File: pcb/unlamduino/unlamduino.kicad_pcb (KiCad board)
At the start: 2 copper layers, 106.7 x 69.8 mm, 41 parts, among them IC2 ATMEGA328-P, P3 CONN_01X08, U1 LM2576, U2 AP111733, Y2 16MHz

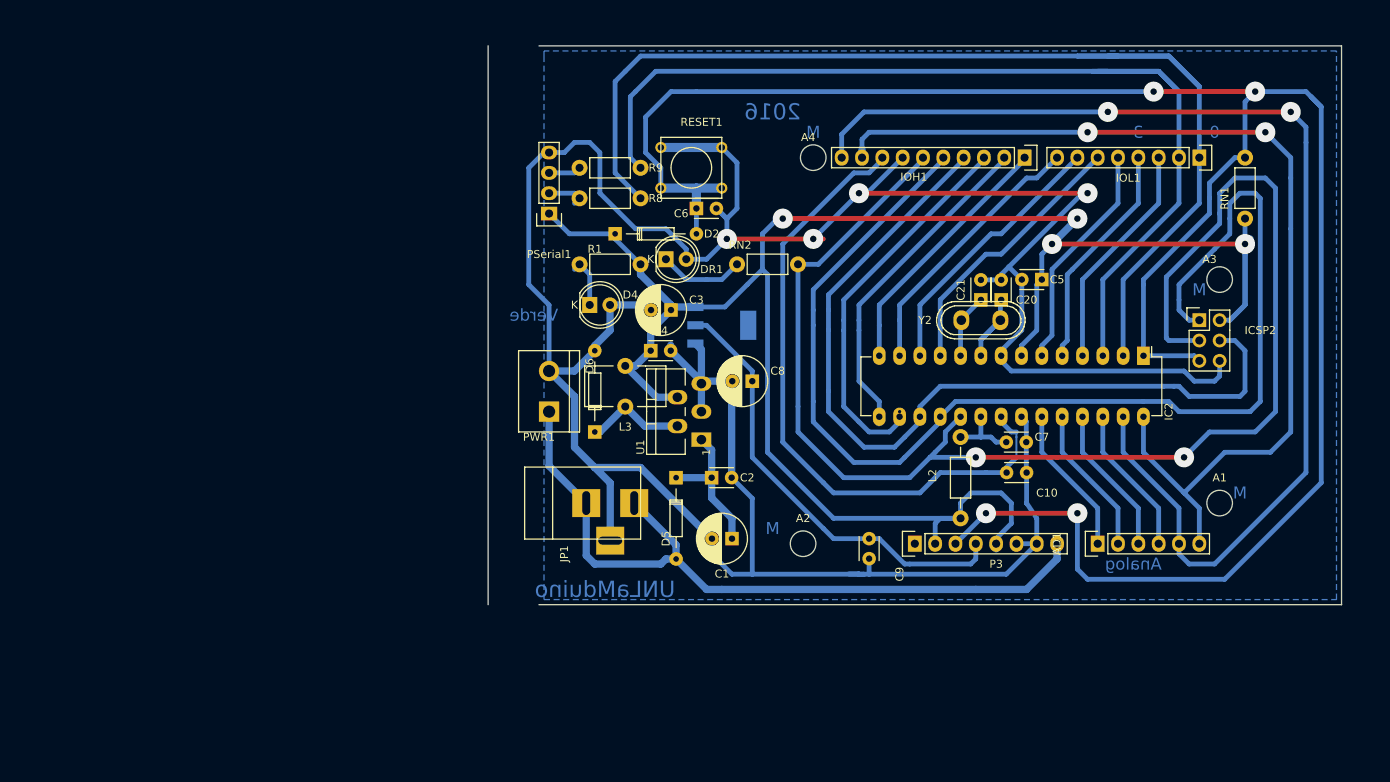
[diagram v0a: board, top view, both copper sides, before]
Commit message: Agregado agujeros de fijación y borde de relleno.
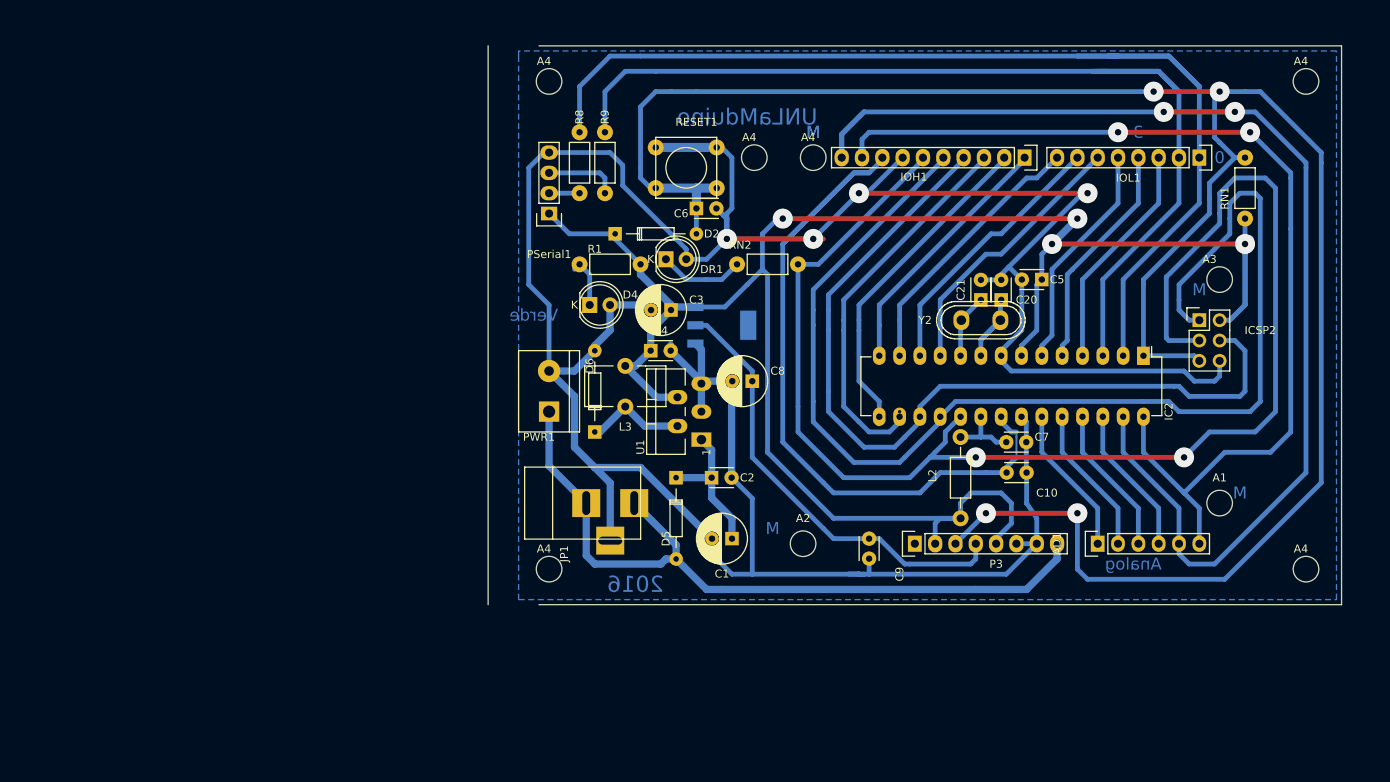
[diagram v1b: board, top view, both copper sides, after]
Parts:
- added A4: Agujero, Mounting_Holes:MountingHole_3.2mm_M3, F.Cu at (254.0, 104.1)
- added A4: Agujero, Mounting_Holes:MountingHole_3.2mm_M3, F.Cu at (159.4, 104.1)
- added A4: Agujero, Mounting_Holes:MountingHole_3.2mm_M3, F.Cu at (185.0, 52.7)
- added A4: Agujero, Mounting_Holes:MountingHole_3.2mm_M3, F.Cu at (159.4, 43.2)
- added A4: Agujero, Mounting_Holes:MountingHole_3.2mm_M3, F.Cu at (254.0, 43.2)
- moved R8 11.2 mm to (163.2, 49.5), turned to 270 degrees
- moved R9 6.29 mm to (166.4, 49.5), turned to 270 degrees
- moved RESET1 0.63 mm to (176.5, 54.0)
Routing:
- net /AD4/SDA: track 147.3 -> 165.3 mm
- net /AREF: track 82.1 -> 96.6 mm
- net /IO0: track 148.2 -> 142.7 mm
- net Net-(PSerial1-Pad3): track 4.07 -> 9.15 mm
- net /RESET: track 265.6 -> 263.0 mm
- net /IO1: track 130.4 -> 129.0 mm
- net Net-(PSerial1-Pad2): track 4.97 -> 3.81 mm
- net /AD5/SCL: track 128.1 -> 127.0 mm

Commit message: Correccion de algunas pistas cerca de islas y limpieza de pistas solapadas.
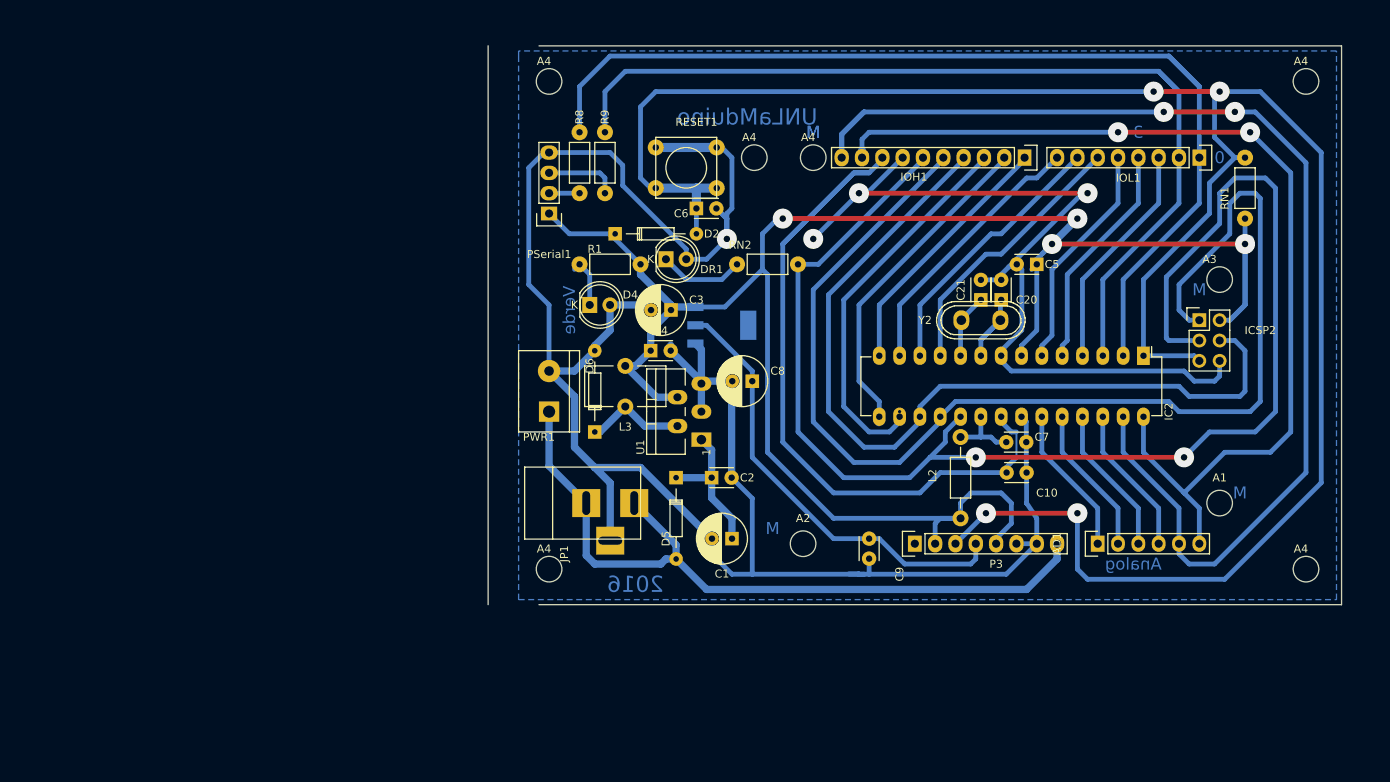
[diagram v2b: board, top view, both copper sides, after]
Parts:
- moved C5 2.01 mm to (220.3, 66.0)
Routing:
- net /IO0: track 142.7 -> 130.0 mm
- net GND: track 391.2 -> 380.1 mm
- net /IO1: track 129.0 -> 119.5 mm
- net /VIN: track 108.6 -> 101.0 mm
- net +5V: track 245.4 -> 248.1 mm

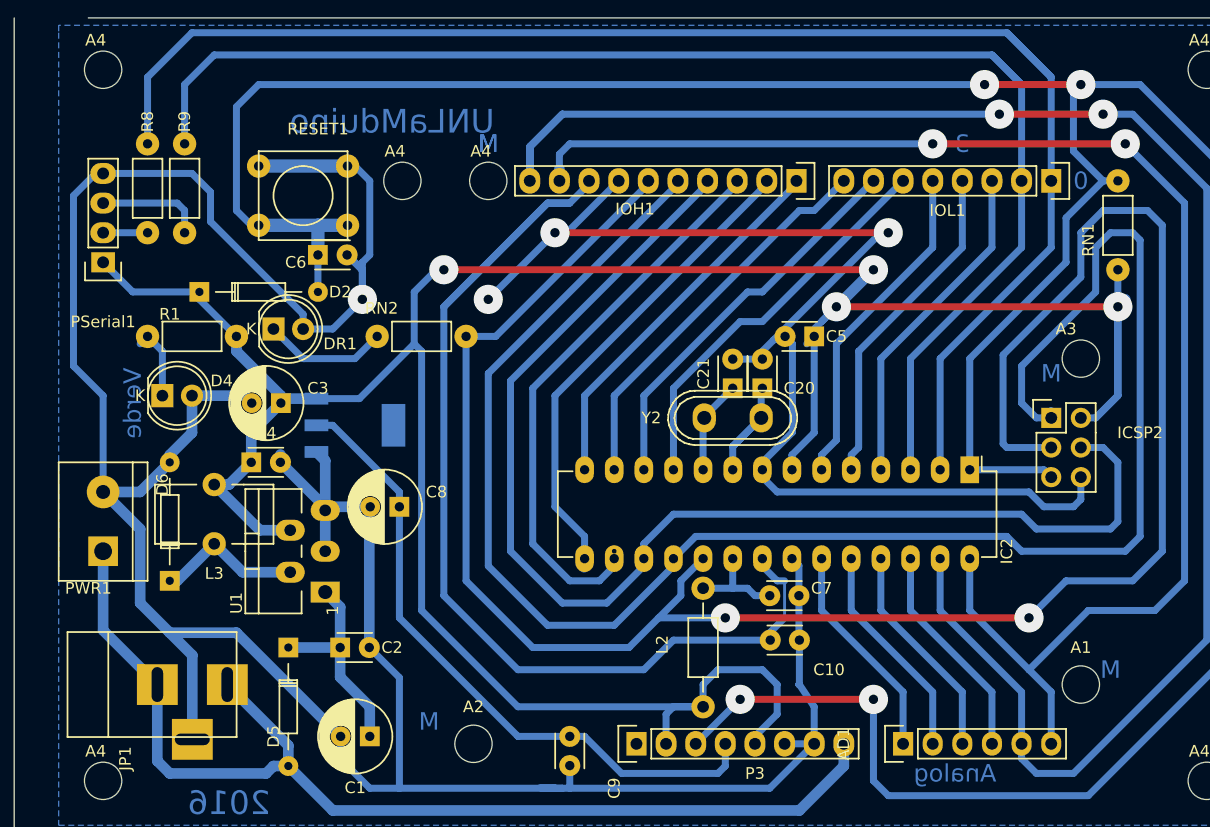
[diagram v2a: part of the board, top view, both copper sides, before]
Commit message: Capacitor mas ancho por pista por el medio y acomodado de alguna pista.
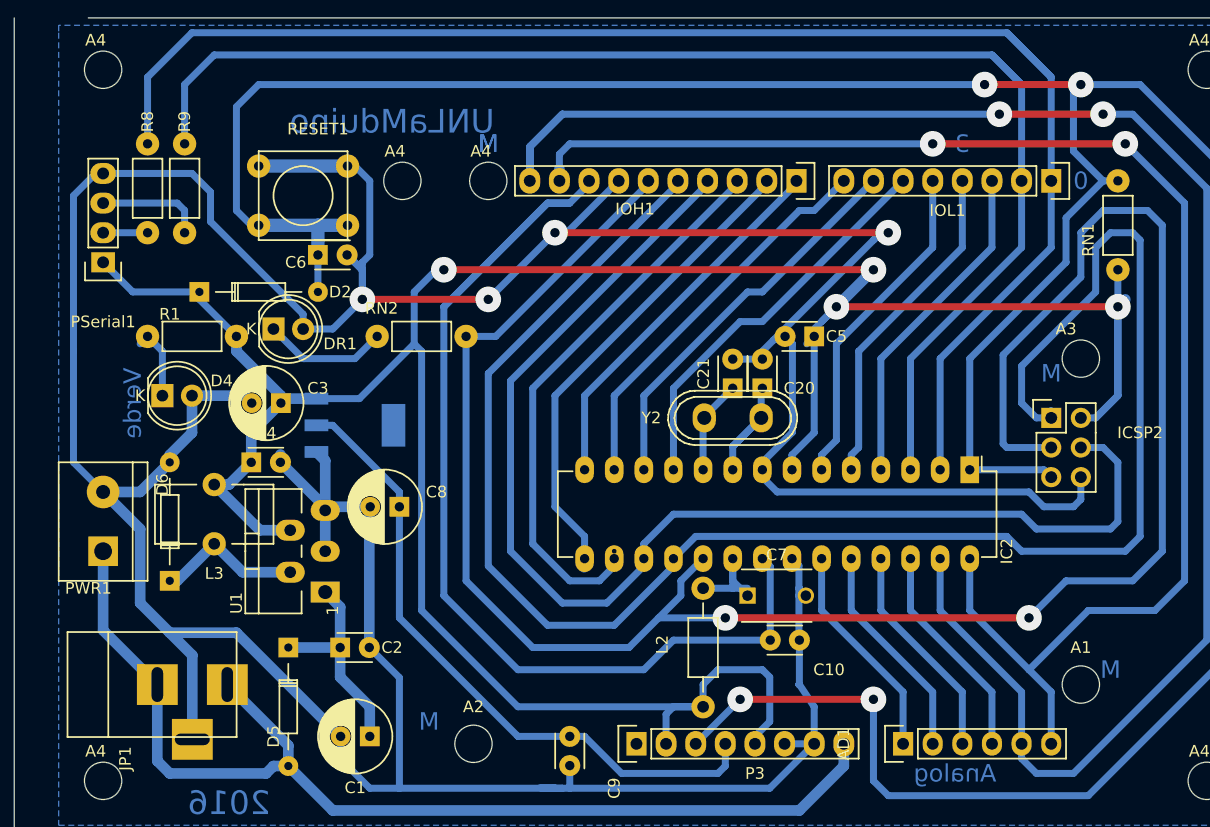
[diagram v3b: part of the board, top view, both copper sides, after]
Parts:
- C7: footprint Capacitors_ThroughHole:C_Disc_D3_P2.5 -> Capacitors_ThroughHole:C_Disc_D6_P5
- moved C7 1.91 mm to (214.6, 88.3)
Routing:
- net GND: track 380.1 -> 393.1 mm
- net Net-(C7-Pad1): track 9.15 -> 10.7 mm
- net +5V: track 248.1 -> 247.0 mm
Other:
- net class Default: via_dia 2.5 -> 2.2

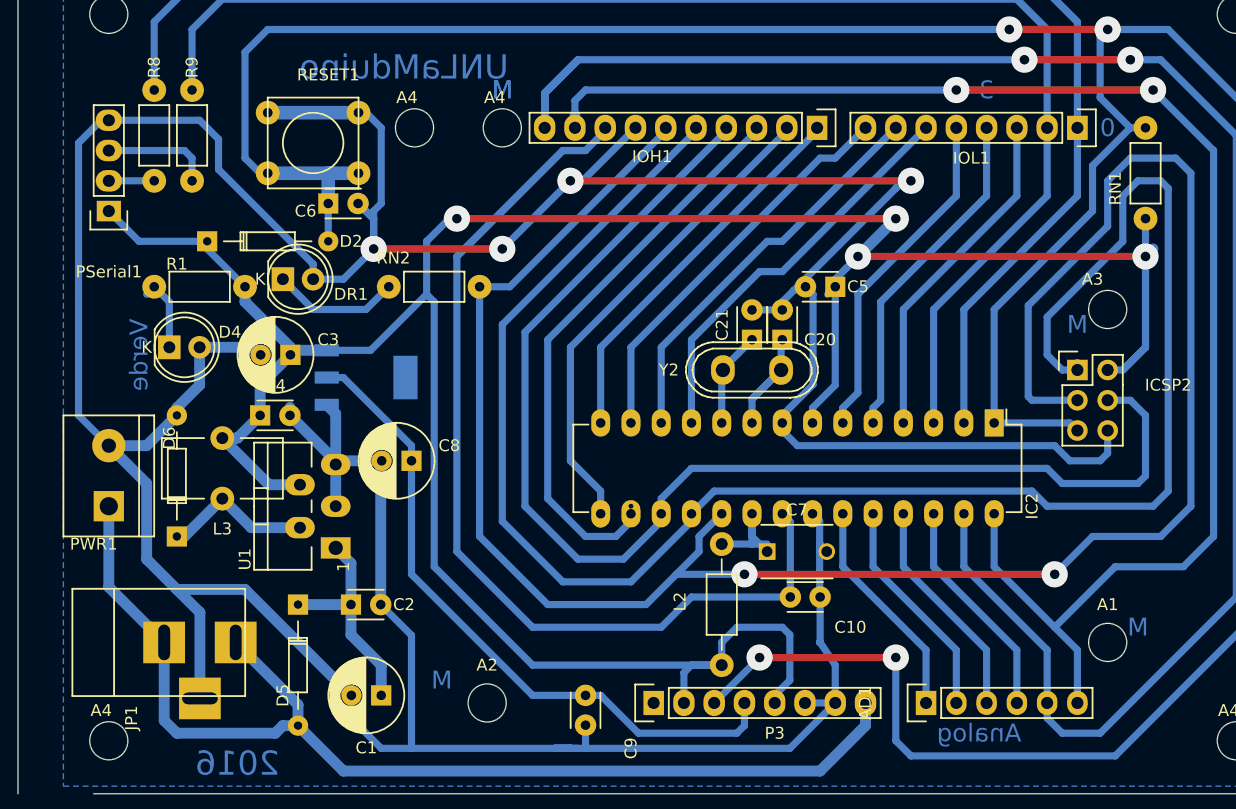
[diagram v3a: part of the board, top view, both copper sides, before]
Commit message: Conector de alimentacion corrido para lugar de agujero.
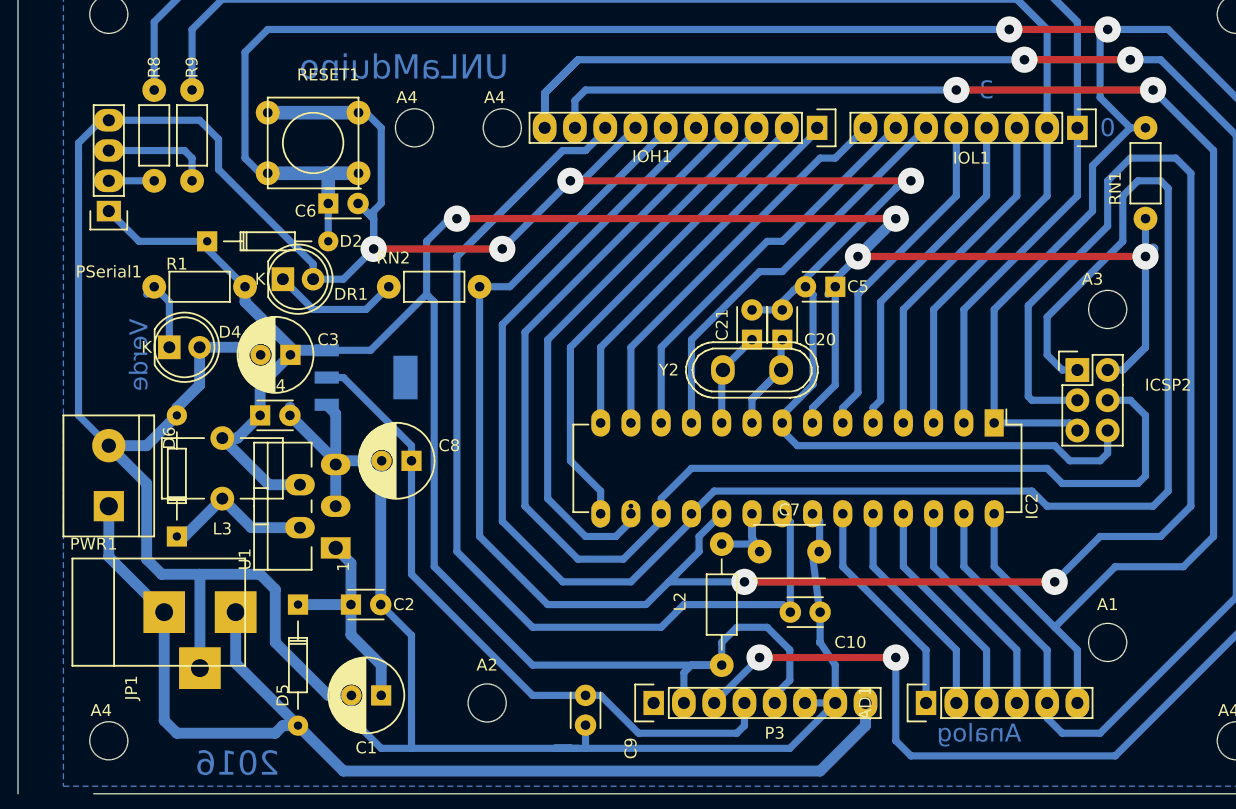
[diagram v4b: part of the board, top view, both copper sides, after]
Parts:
- moved JP1 2.54 mm to (163.8, 93.3)
- moved C10 1.27 mm to (219.1, 93.3)
- moved C7 0.63 mm to (214.0, 88.3)
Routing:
- net /VIN: track 101.0 -> 103.5 mm
- net /AREF: track 96.5 -> 97.8 mm
- net GND: track 393.1 -> 394.3 mm
- net Net-(C7-Pad1): track 10.7 -> 9.67 mm
- net /IO13: track 176.4 -> 177.3 mm
- net +5V: track 247.0 -> 246.2 mm
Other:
- board text removed: "M"

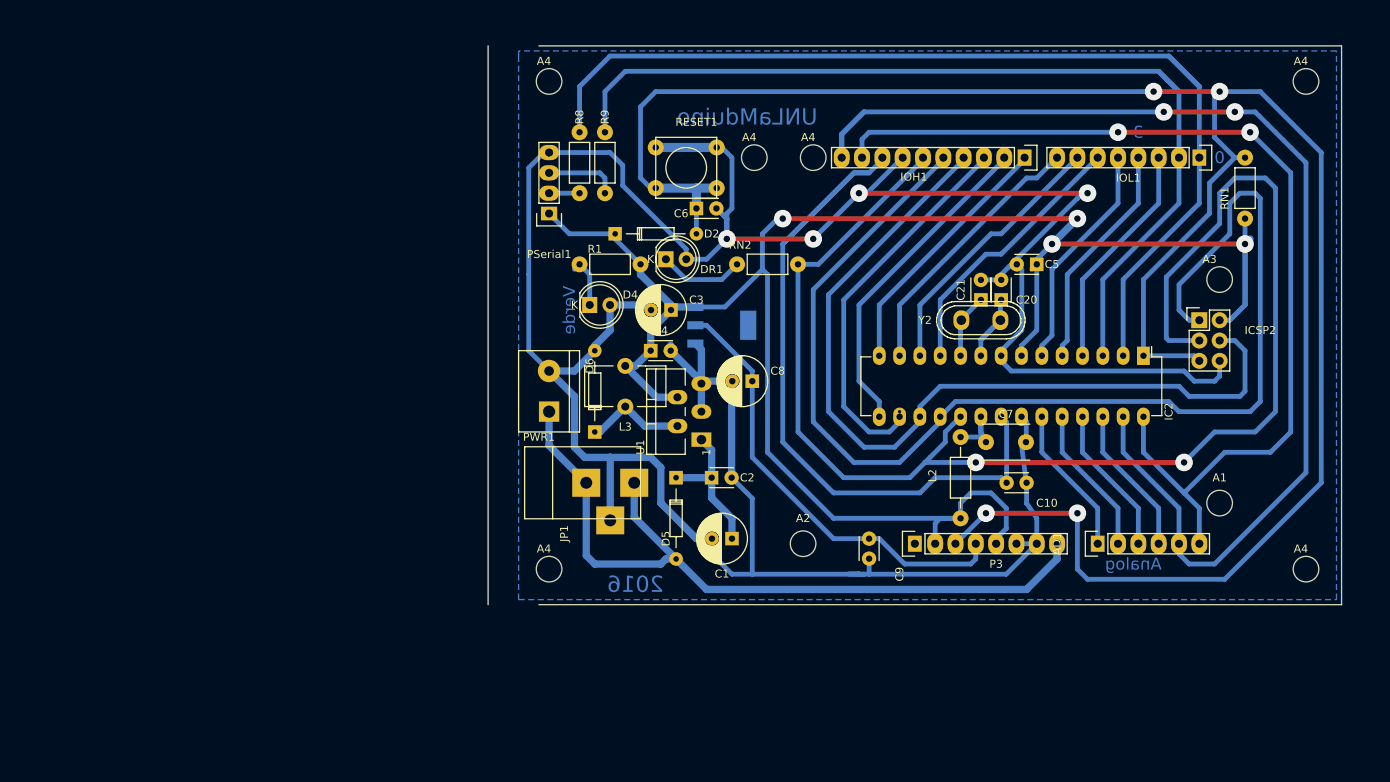
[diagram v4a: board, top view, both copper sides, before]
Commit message: unlamduino pcb: Ordeno serigrafía. Coloco borde adecuado. Muevo límite de zona de relleno. Numero aducuadamente los agujeros.
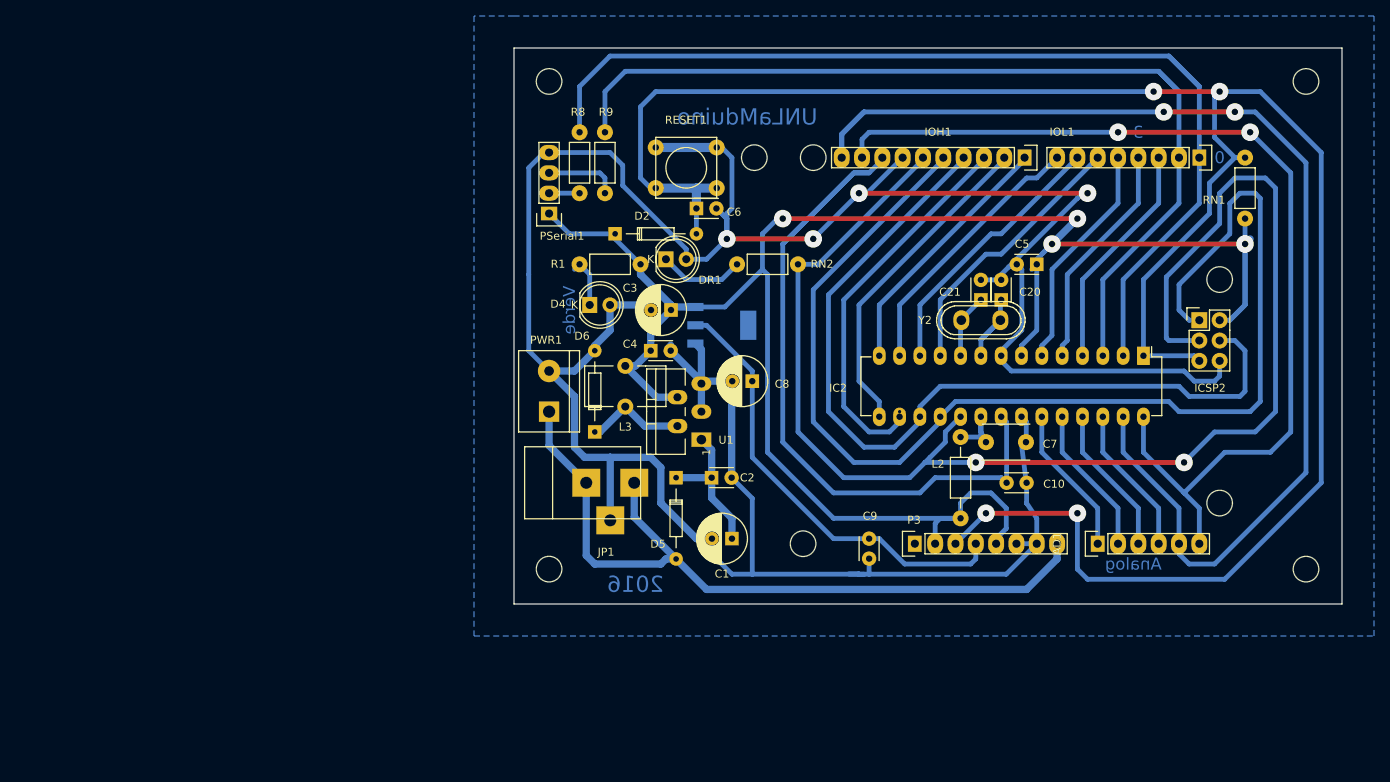
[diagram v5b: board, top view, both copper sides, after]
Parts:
- renumbered A4 to A1, A4 to A2, A4 to A3, A4 to A5, A4 to A6, A3 to A7, A2 to A8, A1 to A9
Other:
- board size 106.7 x 69.8 mm -> 103.5 x 69.5 mm
